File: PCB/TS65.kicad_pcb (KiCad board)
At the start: 2 copper layers, 299.5 x 105.9 mm, 437 parts, among them J1 Programming, J2 INTERCONNECT, J3 INTERCONNECT, J4 UART, J5 I2C, J6 JOYSTICK, P1 USB_CONN, P7_1 5PIN, P7_2 5PIN, Q1 NTR1P02T1G - PMOS, Q2 NDS332P, U2 MCP23018, U3 IP4234CZ6, U5 PAM2804, U6 AP1117-33, U7 STM32F303CCTx, Y1 8M ABM2-8.000MHZ-D4Y-T

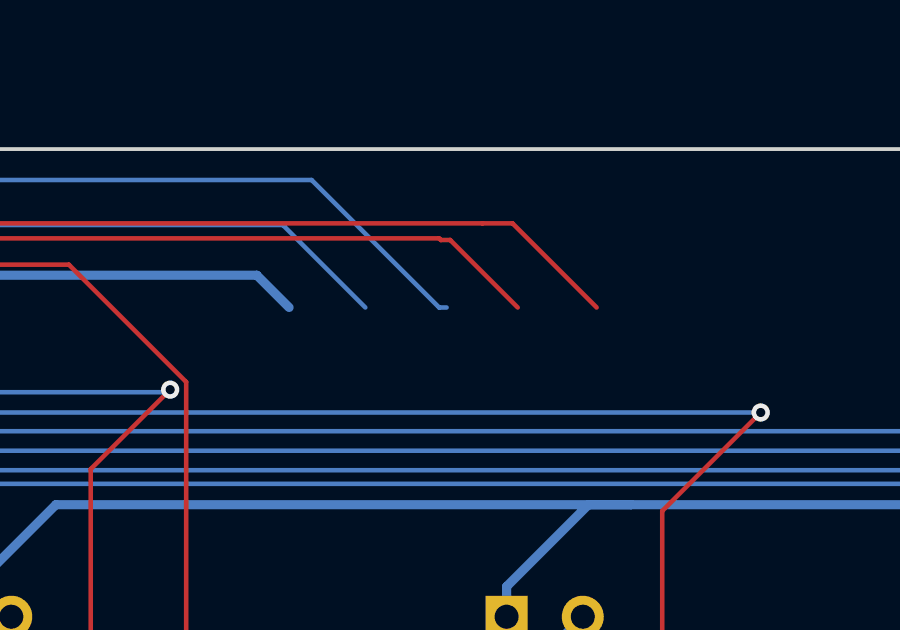
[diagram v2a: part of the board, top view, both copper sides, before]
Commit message: Updating to re-include expansion port from left side.
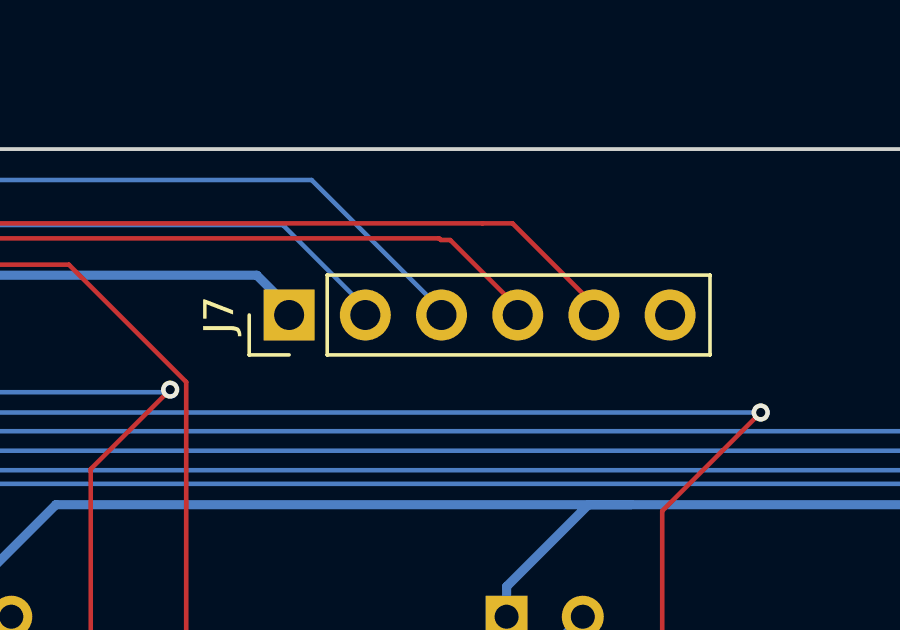
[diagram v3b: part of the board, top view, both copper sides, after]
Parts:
- added J7: EXPANSION, Connector_PinHeader_2.54mm:PinHeader_1x06_P2.54mm_Vertical, F.Cu at (289.2, 73.3)
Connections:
- U2 pad 8: (no net) -> /mcu/GPIO_A
- U2 pad 9: (no net) -> /mcu/GPIO_B
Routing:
- net (no net): track 97.1 -> 0.00 mm, vias 2 -> 0
- net /mcu/GPIO_B: track 0.00 -> 49.9 mm, vias 0 -> 1
- net /mcu/GPIO_A: track 0.00 -> 47.2 mm, vias 0 -> 1
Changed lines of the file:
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@@
     (tracks 4194)
     (zones 0)
-    (modules 437)
-    (nets 175)
+    (modules 438)
+    (nets 177)
   )
   (page A3)
@@
   (net 173 /mcu/JOY_Y)
   (net 174 /mcu/JOY_X)
+  (net 175 /mcu/GPIO_A)
+  (net 176 /mcu/GPIO_B)
   (net_class Default "This is the default net class."
     (clearance 0.1524)
@@
     (add_net /mcu/ENCA)
     (add_net /mcu/ENCB)
+    (add_net /mcu/GPIO_A)
+    (add_net /mcu/GPIO_B)
     (add_net /mcu/JOY_X)
     (add_net /mcu/JOY_Y)
@@
     (add_net VSS)
   )
+  (module Connector_PinHeader_2.54mm:PinHeader_1x06_P2.54mm_Vertical (layer Front)
+    (at 289.207 73.331 90)
+    (descr "Through hole straight pin header, 1x06, 2.54mm pitch, single row")
+    (tags "Through hole pin header THT 1x06 2.54mm single row")
+    (fp_text reference J7 (at 0 -2.33 90) (layer F.SilkS)
+      (effects (font (size 1 1) (thickness 0.15)))
+    )
+    (fp_text value EXPANSION (at 0 15.03 90) (layer F.Fab)
+      (effects (font (size 1 1) (thickness 0.15)))
+    )
+    (fp_text user %R (at 0 6.35 180) (layer F.Fab)
+      (effects (font (size 1 1) (thickness 0.15)))
+    )
+    (fp_line (start 1.8 -1.8) (end -1.8 -1.8) (layer F.CrtYd) (width 0.05))
+    (fp_line (start 1.8 14.5) (end 1.8 -1.8) (layer F.CrtYd) (width 0.05))
+    (fp_line (start -1.8 14.5) (end 1.8 14.5) (layer F.CrtYd) (width 0.05))
+    (fp_line (start -1.8 -1.8) (end -1.8 14.5) (layer F.CrtYd) (width 0.05))
+    (fp_line (start -1.33 -1.33) (end 0 -1.33) (layer F.SilkS) (width 0.12))
+    (fp_line (start -1.33 0) (end -1.33 -1.33) (layer F.SilkS) (width 0.12))
+    (fp_line (start -1.33 1.27) (end 1.33 1.27) (layer F.SilkS) (width 0.12))
+    (fp_line (start 1.33 1.27) (end 1.33 14.03) (layer F.SilkS) (width 0.12))
+    (fp_line (start -1.33 1.27) (end -1.33 14.03) (layer F.SilkS) (width 0.12))
+    (fp_line (start -1.33 14.03) (end 1.33 14.03) (layer F.SilkS) (width 0.12))
+    (fp_line (start -1.27 -0.635) (end -0.635 -1.27) (layer F.Fab) (width 0.1))
+    (fp_line (start -1.27 13.97) (end -1.27 -0.635) (layer F.Fab) (width 0.1))
+    (fp_line (start 1.27 13.97) (end -1.27 13.97) (layer F.Fab) (width 0.1))
+    (fp_line (start 1.27 -1.27) (end 1.27 13.97) (layer F.Fab) (width 0.1))
+    (fp_line (start -0.635 -1.27) (end 1.27 -1.27) (layer F.Fab) (width 0.1))
+    (pad 6 thru_hole oval (at 0 12.7 90) (size 1.7 1.7) (drill 1) (layers *.Cu *.Mask)
+      (net 1 VSS))
+    (pad 5 thru_hole oval (at 0 10.16 90) (size 1.7 1.7) (drill 1) (layers *.Cu *.Mask)
+      (net 176 /mcu/GPIO_B))
+    (pad 4 thru_hole oval (at 0 7.62 90) (size 1.7 1.7) (drill 1) (layers *.Cu *.Mask)
+      (net 175 /mcu/GPIO_A))
+    (pad 3 thru_hole oval (at 0 5.08 90) (size 1.7 1.7) (drill 1) (layers *.Cu *.Mask)
+      (net 37 /mcu/SDA_))
+    (pad 2 thru_hole oval (at 0 2.54 90) (size 1.7 1.7) (drill 1) (layers *.Cu *.Mask)
+      (net 38 /mcu/SCL_))
+    (pad 1 thru_hole rect (at 0 0 90) (size 1.7 1.7) (drill 1) (layers *.Cu *.Mask)
+      (net 163 +3V3))
+    (model ${KISYS3DMOD}/Connector_PinHeader_2.54mm.3dshapes/PinHeader_1x06_P2.54mm_Vertical.wrl
+      (at (xyz 0 0 0))
+      (scale (xyz 1 1 1))
+      (rotate (xyz 0 0 0))
+    )
+  )
   (module Connector_PinHeader_2.54mm:PinHeader_1x04_P2.54mm_Vertical (layer Front)
     (at 192.957 85.751)
@@
     (pad 7 smd rect (at -3.6 -0.325) (size 1.75 0.45) (layers Back B.Paste B.Mask)
       (net 146 /RowR5))
-    (pad 8 smd rect (at -3.6 -0.975) (size 1.75 0.45) (layers Back B.Paste B.Mask))
-    (pad 9 smd rect (at -3.6 -1.625) (size 1.75 0.45) (layers Back B.Paste B.Mask))
+    (pad 8 smd rect (at -3.6 -0.975) (size 1.75 0.45) (layers Back B.Paste B.Mask)
+      (net 175 /mcu/GPIO_A))
+    (pad 9 smd rect (at -3.6 -1.625) (size 1.75 0.45) (layers Back B.Paste B.Mask)
+      (net 176 /mcu/GPIO_B))
     (pad 10 smd rect (at -3.6 -2.275) (size 1.75 0.45) (layers Back B.Paste B.Mask)
       (net 163 +3V3))
@@
   (gr_line (start 213.7 100.8) (end 205.8 100.8) (layer Edge.Cuts) (width 0.127))
   (gr_line (start 214.5 85.4) (end 214.5 100) (layer Edge.Cuts) (width 0.127))
+  (via (at 257.207 71.081) (size 0.6096) (drill 0.3048) (layers Front Back) (net 175))
+  (segment (start 257.207 71.081) (end 257.511799 70.776201) (width 0.1524) (layer Front) (net 175))
+  (segment (start 251.924 73.955) (end 253.264067 73.955) (width 0.1524) (layer Back) (net 175))
+  (segment (start 253.264067 73.955) (end 255.833268 71.385799) (width 0.1524) (layer Back) (net 175))
+  (segment (start 256.902201 71.385799) (end 257.207 71.081) (width 0.1524) (layer Back) (net 175))
+  (segment (start 255.833268 71.385799) (end 256.902201 71.385799) (width 0.1524) (layer Back) (net 175))
+  (segment (start 294.577 70.831) (end 294.261799 70.831) (width 0.1524) (layer Front) (net 175))
+  (segment (start 296.827 73.081) (end 294.577 70.831) (width 0.1524) (layer Front) (net 175))
+  (segment (start 257.511799 70.776201) (end 294.207 70.776201) (width 0.1524) (layer Front) (net 175))
+  (segment (start 294.261799 70.831) (end 294.207 70.776201) (width 0.1524) (layer Front) (net 175))
+  (segment (start 253.483 73.305) (end 256.207 70.581) (width 0.1524) (layer Back) (net 176))
+  (segment (start 251.924 73.305) (end 253.483 73.305) (width 0.1524) (layer Back) (net 176))
+  (via (at 256.207 70.581) (size 0.6096) (drill 0.3048) (layers Front Back) (net 176))
+  (segment (start 256.511799 70.276201) (end 295.652201 70.276201) (width 0.1524) (layer Front) (net 176))
+  (segment (start 256.207 70.581) (end 256.511799 70.276201) (width 0.1524) (layer Front) (net 176))
+  (segment (start 295.652201 70.276201) (end 296.652201 70.276201) (width 0.1524) (layer Front) (net 176))
+  (segment (start 296.652201 70.276201) (end 299.457 73.081) (width 0.1524) (layer Front) (net 176))
   (segment (start 86.2805 98.282) (end 86.0552 98.0567) (width 0.3048) (layer Back) (net 1))
   (segment (start 88.646 94.145848) (end 86.0552 96.736648) (width 0.3048) (layer Front) (net 1))
@@
   (segment (start 144.825989 76.738819) (end 141.41817 73.331) (width 0.1524) (layer Back) (net 174))
   (segment (start 151.43349 79.376423) (end 146.963594 79.376423) (width 0.1524) (layer Back) (net 174))
-  (via (at 257.207 71.081) (size 0.6096) (drill 0.3048) (layers Front Back) (net 0))
-  (segment (start 257.207 71.081) (end 257.511799 70.776201) (width 0.1524) (layer Front) (net 0))
-  (segment (start 251.924 73.955) (end 253.264067 73.955) (width 0.1524) (layer Back) (net 0))
-  (segment (start 253.264067 73.955) (end 255.833268 71.385799) (width 0.1524) (layer Back) (net 0))
-  (segment (start 256.902201 71.385799) (end 257.207 71.081) (width 0.1524) (layer Back) (net 0))
-  (segment (start 255.833268 71.385799) (end 256.902201 71.385799) (width 0.1524) (layer Back) (net 0))
-  (segment (start 294.577 70.831) (end 294.261799 70.831) (width 0.1524) (layer Front) (net 0))
-  (segment (start 296.827 73.081) (end 294.577 70.831) (width 0.1524) (layer Front) (net 0))
-  (segment (start 257.511799 70.776201) (end 294.207 70.776201) (width 0.1524) (layer Front) (net 0))
-  (segment (start 294.261799 70.831) (end 294.207 70.776201) (width 0.1524) (layer Front) (net 0))
-  (segment (start 253.483 73.305) (end 256.207 70.581) (width 0.1524) (layer Back) (net 0))
-  (segment (start 251.924 73.305) (end 253.483 73.305) (width 0.1524) (layer Back) (net 0))
-  (via (at 256.207 70.581) (size 0.6096) (drill 0.3048) (layers Front Back) (net 0))
-  (segment (start 256.511799 70.276201) (end 295.652201 70.276201) (width 0.1524) (layer Front) (net 0))
-  (segment (start 256.207 70.581) (end 256.511799 70.276201) (width 0.1524) (layer Front) (net 0))
-  (segment (start 295.652201 70.276201) (end 296.652201 70.276201) (width 0.1524) (layer Front) (net 0))
-  (segment (start 296.652201 70.276201) (end 299.457 73.081) (width 0.1524) (layer Front) (net 0))
   (zone (net 1) (net_name VSS) (layer Front) (hatch edge 0.508)
     (connect_pads (clearance 0.308))
